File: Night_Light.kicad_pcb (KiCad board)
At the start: 2 copper layers, 25.4 x 25.4 mm, 6 parts, among them J1 3V0, Q1 2N3904

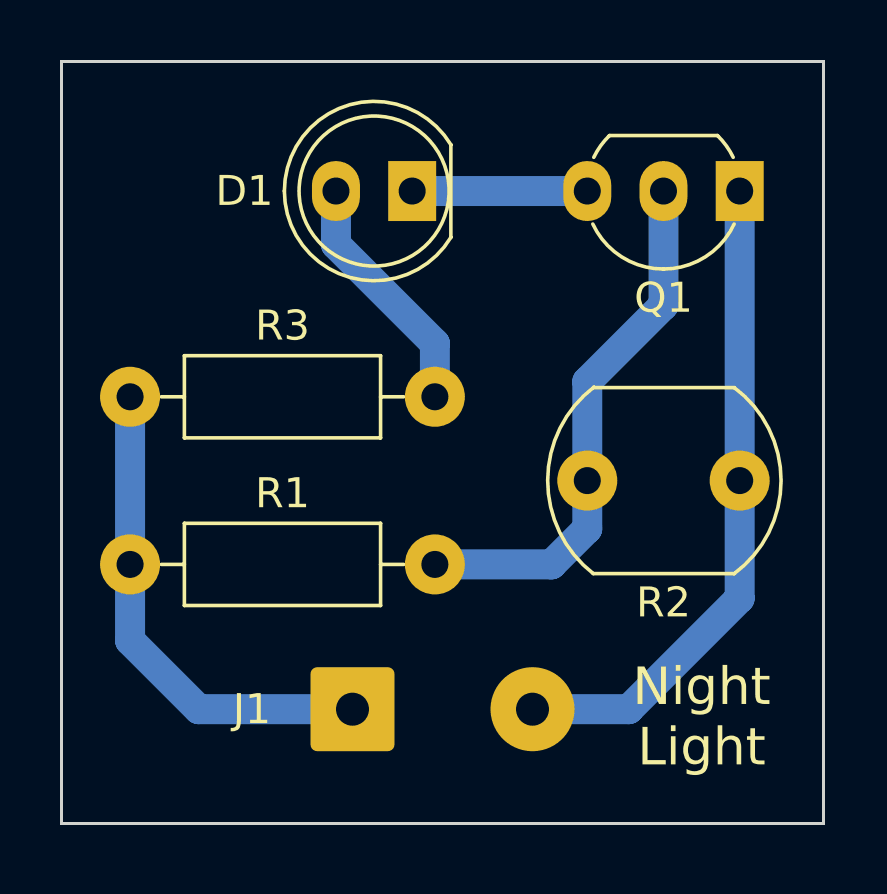
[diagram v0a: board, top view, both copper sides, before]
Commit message: Update silkscreen. Fixes #7, #8, #9, and #11
- Change "D1" label to "LED1". #7
- Make silkscreen text bigger and thicker. #8
- Add "+" and "-" to power pads. #9
- Add LED polarity to silkscreen. #11
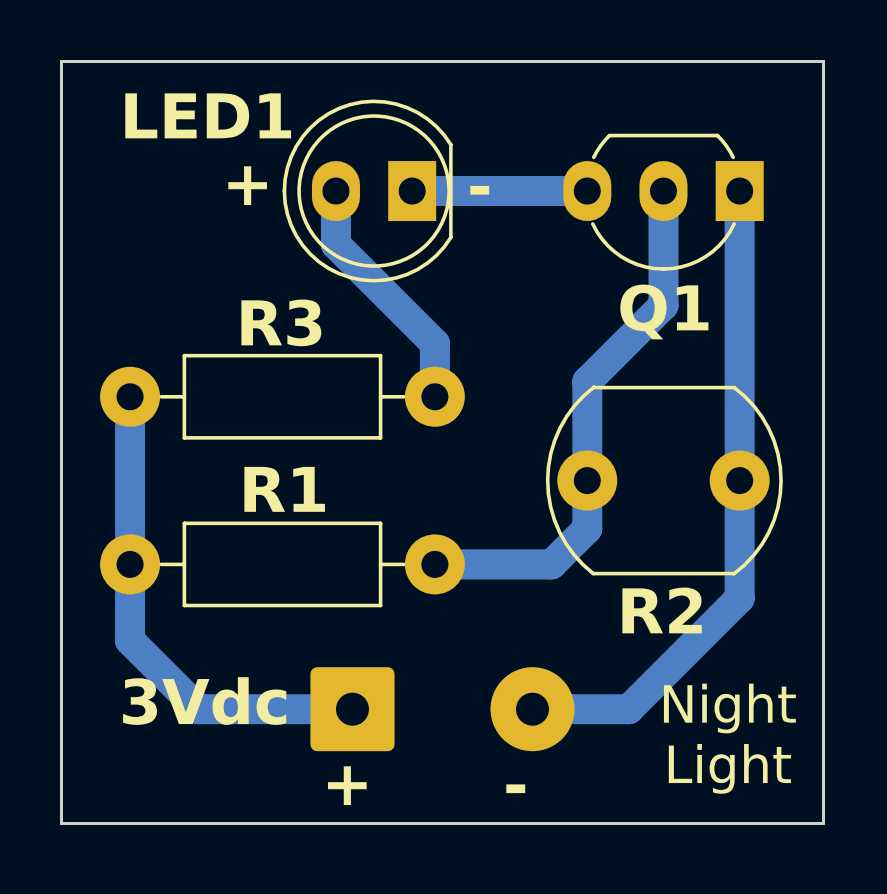
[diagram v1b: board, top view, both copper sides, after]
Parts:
- renumbered D1 to LED1
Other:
- board text added: "+"
- board text added: "-"
- board text added: "3Vdc"
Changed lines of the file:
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@@
     (property "ki_keywords" "LED diode")
     (attr through_hole)
-    (fp_text reference "D1" (at 5.593 0) (layer "F.SilkS")
-        (effects (font (size 1 1) (thickness 0.1524)))
+    (fp_text reference "LED1" (at 6.823 2.45) (layer "F.SilkS")
+        (effects (font (size 1.5 1.5) (thickness 0.25) bold))
     )
     (fp_text value "White" (at 1.27 3.96) (layer "F.Fab")
@@
     (property "ki_keywords" "R res resistor")
     (attr through_hole)
-    (fp_text reference "R3" (at 5.08 -2.37) (layer "F.SilkS")
-        (effects (font (size 1 1) (thickness 0.1524)))
+    (fp_text reference "R3" (at 5.03 -2.408) (layer "F.SilkS")
+        (effects (font (size 1.5 1.5) (thickness 0.25) bold))
     )
     (fp_text value "100R" (at 5.08 2.37) (layer "F.Fab")
@@
     (property "ki_keywords" "transistor NPN")
     (attr through_hole)
-    (fp_text reference "Q1" (at 2.54 -3.56 180) (layer "F.SilkS")
-        (effects (font (size 1 1) (thickness 0.1524)))
+    (fp_text reference "Q1" (at 2.49 -3.95 180) (layer "F.SilkS")
+        (effects (font (size 1.5 1.5) (thickness 0.25) bold))
     )
     (fp_text value "2N3904" (at 2.54 2.79 180) (layer "F.Fab")
@@
     (property "ki_keywords" "connector")
     (attr exclude_from_pos_files)
-    (fp_text reference "J1" (at -3.35 0) (layer "F.SilkS")
-        (effects (font (size 1 1) (thickness 0.1524)))
+    (fp_text reference "J1" (at -4.084 -0.022) (layer "F.SilkS") hide
+        (effects (font (size 1.5 1.5) (thickness 0.25) bold))
     )
     (fp_text value "3V0" (at 3 2.75) (layer "F.Fab")
@@
     (property "ki_keywords" "R res resistor")
     (attr through_hole)
-    (fp_text reference "R1" (at 5.08 -2.37) (layer "F.SilkS")
-        (effects (font (size 1 1) (thickness 0.1524)))
+    (fp_text reference "R1" (at 5.13 -2.446) (layer "F.SilkS")
+        (effects (font (size 1.5 1.5) (thickness 0.25) bold))
     )
     (fp_text value "10K" (at 5.08 2.37) (layer "F.Fab")
@@
     (property "ki_keywords" "resistor variable light sensitive opto LDR")
     (attr through_hole)
-    (fp_text reference "R2" (at 2.54 4.064) (layer "F.SilkS")
-        (effects (font (size 1 1) (thickness 0.1524)))
+    (fp_text reference "R2" (at 2.49 4.398) (layer "F.SilkS")
+        (effects (font (size 1.5 1.5) (thickness 0.25) bold))
     )
     (fp_text value "8K-200K" (at 2.54 4.06) (layer "F.Fab")
@@
     (effects (font (size 1 1) (thickness 0.1524)) (justify mirror))
   )
-  (gr_text "Night\nLight" (at 148.336 98.044) (layer "F.SilkS")
+  (gr_text "+" (at 135.666 101.168) (layer "F.SilkS")
+    (effects (font (size 1.5 1.5) (thickness 0.25) bold) (justify left bottom))
+  )
+  (gr_text "-" (at 141.716 101.218) (layer "F.SilkS")
+    (effects (font (size 1.5 1.5) (thickness 0.25) bold) (justify left bottom))
+  )
+  (gr_text "Night\nLight" (at 149.216 98.668) (layer "F.SilkS")
     (effects (font (size 1.25 1.25) (thickness 0.2)))
   )
+  (gr_text "3Vdc" (at 128.916 98.468) (layer "F.SilkS")
+    (effects (font (size 1.5 1.5) (thickness 0.25) bold) (justify left bottom))
+  )
+  (gr_text "-" (at 140.516 81.268) (layer "F.SilkS")
+    (effects (font (size 1.5 1.5) (thickness 0.25) bold) (justify left bottom))
+  )
+  (gr_text "+" (at 134.066 81.168) (layer "F.SilkS")
+    (effects (font (size 1.5 1.5) (thickness 0.25) bold) (justify left bottom mirror))
+  )
   (segment (start 138.689 80.518) (end 144.526 80.518) (width 1) (layer "B.Cu") (net 1))

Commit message: Update version to 1.1.0
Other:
- board text added: "v1.1.0"
- board text removed: "v1.0.0"
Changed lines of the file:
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@@
   (title_block
     (title "Night Light")
-    (date "2023-02-14")
-    (rev "1.0.0")
+    (date "2023-04-16")
+    (rev "1.1.0")
     (company "Julian Jayhawks")
     (comment 1 "Zach \"Chef\" Dribin")
@@
   (gr_rect (start 127 76.2) (end 152.4 101.6)
     (stroke (width 0.1) (type solid)) (fill none) (layer "Edge.Cuts"))
-  (gr_text "v1.0.0" (at 148.336 98.044) (layer "B.SilkS")
+  (gr_text "v1.1.0" (at 148.336 98.044) (layer "B.SilkS")
     (effects (font (size 1 1) (thickness 0.1524)) (justify mirror))
   )

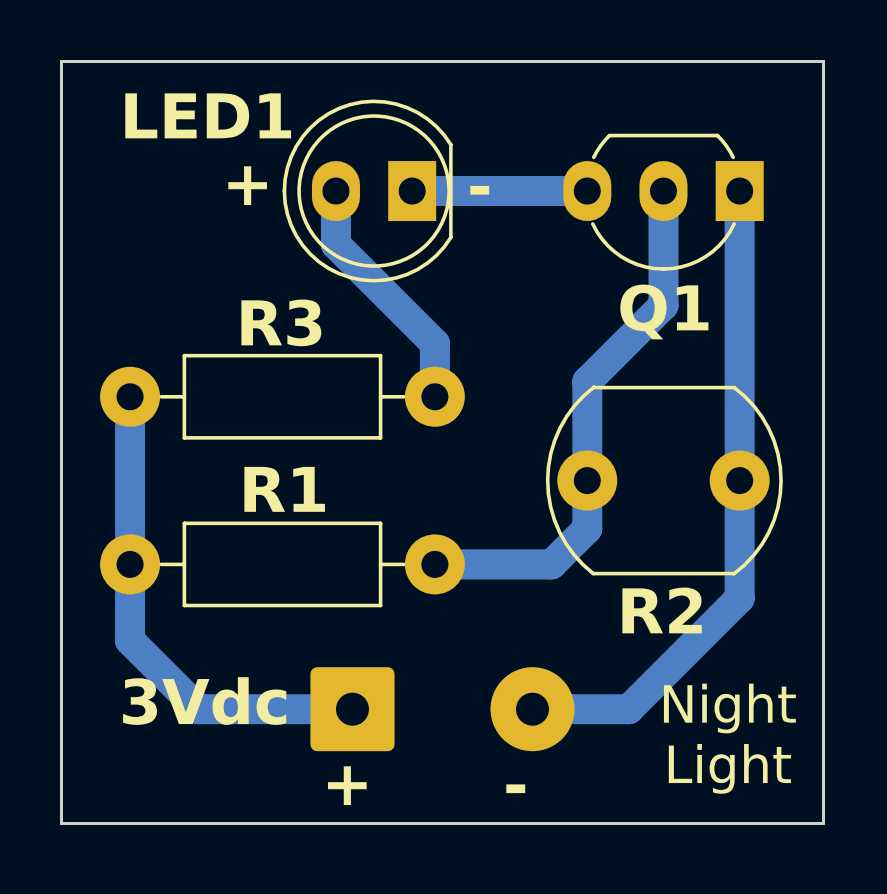
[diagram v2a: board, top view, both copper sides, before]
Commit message: Change R3 and add resistor values to silkscreen
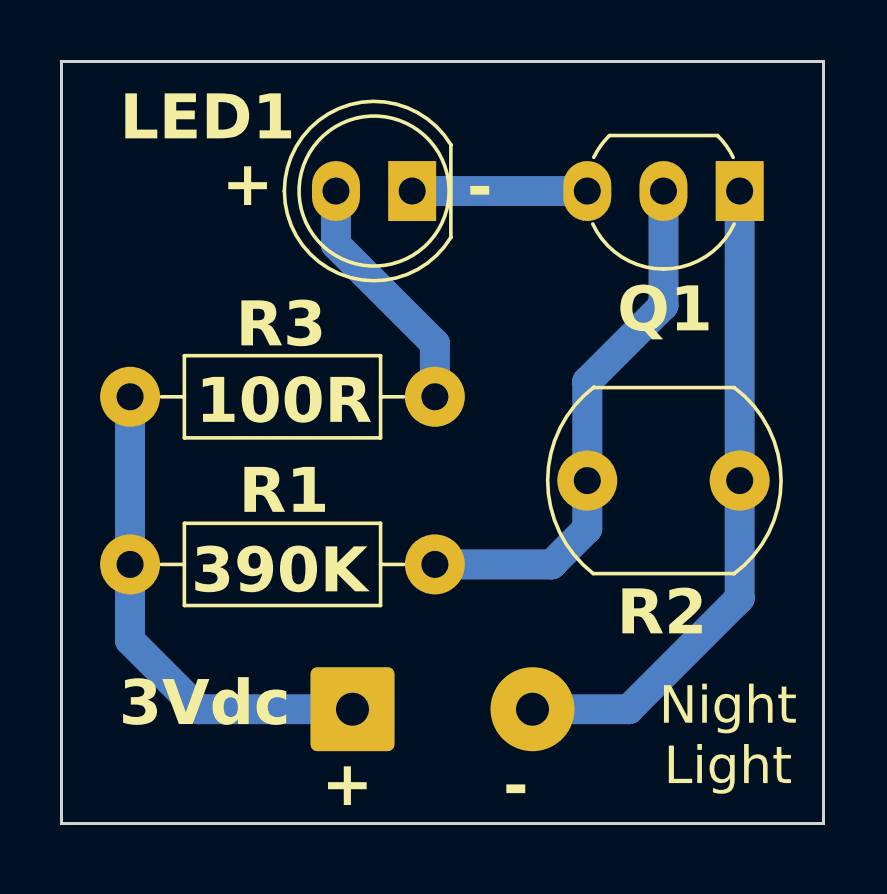
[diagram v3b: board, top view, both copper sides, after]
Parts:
- R1: value 10K -> 390K
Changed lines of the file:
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@@
         (effects (font (size 1.5 1.5) (thickness 0.25) bold))
     )
-    (fp_text value "100R" (at 5.08 2.37) (layer "F.Fab")
-        (effects (font (size 1 1) (thickness 0.15)))
+    (fp_text value "100R" (at 5.13 0.142) (layer "F.SilkS")
+        (effects (font (size 1.5 1.5) (thickness 0.25) bold))
     )
     (fp_text user "${REFERENCE}" (at 5.08 0) (layer "F.Fab")
@@
         (effects (font (size 1.5 1.5) (thickness 0.25) bold))
     )
-    (fp_text value "10K" (at 5.08 2.37) (layer "F.Fab")
-        (effects (font (size 1 1) (thickness 0.15)))
+    (fp_text value "390K" (at 4.98 0.204) (layer "F.SilkS")
+        (effects (font (size 1.5 1.5) (thickness 0.25) bold))
     )
     (fp_text user "${REFERENCE}" (at 5.08 0) (layer "F.Fab")

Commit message: Copy all updated footprints into a project footprint library, to avoid DRC warnings
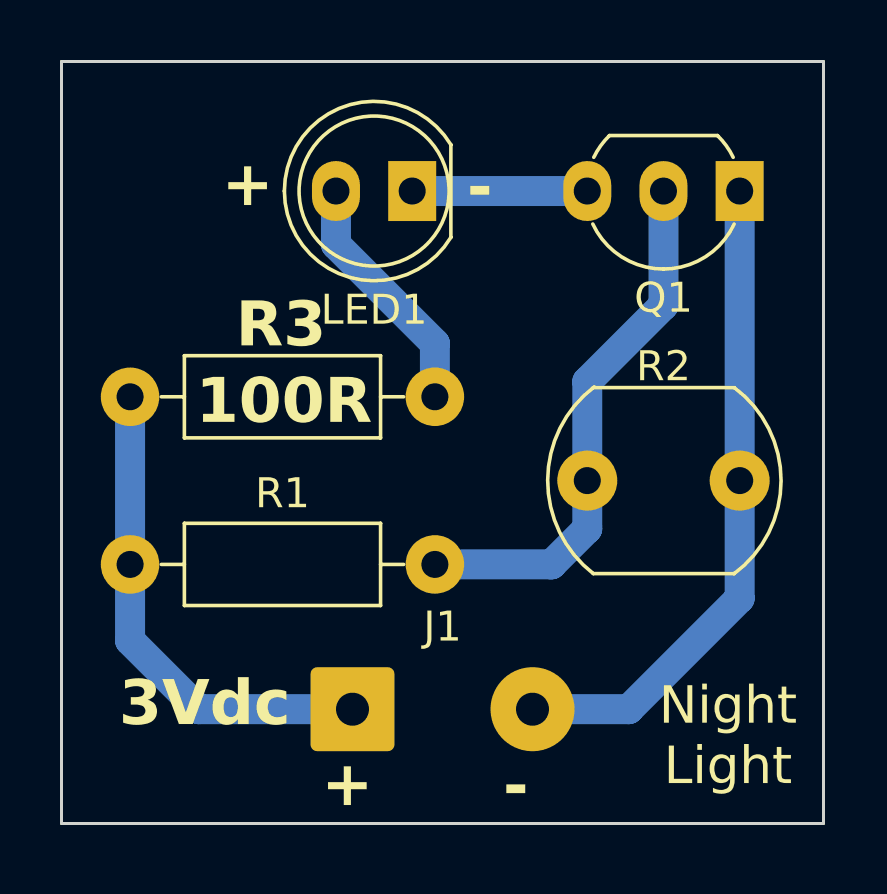
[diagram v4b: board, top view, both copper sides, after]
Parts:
- J1: footprint Connector_Wire:SolderWire-1.5sqmm_1x02_P6mm_D1.7mm_OD3mm -> 00_Project:SolderWire-1.5sqmm_1x02_P6mm_D1.7mm_OD3mm
- LED1: footprint LED_THT:LED_D5.0mm_Clear -> 00_Project:LED_D5.0mm_Clear
- Q1: footprint Package_TO_SOT_THT:TO-92_Inline_Wide -> 00_Project:TO-92_Inline_Wide
- R1, R3: footprint Resistor_THT:R_Axial_DIN0207_L6.3mm_D2.5mm_P10.16mm_Horizontal -> 00_Project:R_Axial_DIN0207_L6.3mm_D2.5mm_P10.16mm_Horizontal
- R2: footprint OptoDevice:R_LDR_7x6mm_P5.1mm_Vertical -> 00_Project:R_LDR_7x6mm_P5.1mm_Vertical
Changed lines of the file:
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@@
   (net 4 "GND")
   (net 5 "/Base")
-  (footprint "LED_THT:LED_D5.0mm_Clear" (layer "F.Cu")
+  (footprint "00_Project:LED_D5.0mm_Clear" (layer "F.Cu")
     (at 138.689 80.518 180)
     (descr "LED, diameter 5.0mm, 2 pins, http://cdn-reichelt.de/documents/datenblatt/A500/LL-504BC2E-009.pdf")
@@
     (property "ki_keywords" "LED diode")
     (attr through_hole)
-    (fp_text reference "LED1" (at 6.823 2.45) (layer "F.SilkS")
-        (effects (font (size 1.5 1.5) (thickness 0.25) bold))
-    )
-    (fp_text value "White" (at 1.27 3.96) (layer "F.Fab")
-        (effects (font (size 1 1) (thickness 0.15)))
-    )
-    (fp_text user "${REFERENCE}" (at 1.25 0) (layer "F.Fab")
+    (fp_text reference "LED1" (at 1.27 -3.96 180) (layer "F.SilkS")
+        (effects (font (size 1 1) (thickness 0.15)))
+    )
+    (fp_text value "White" (at 1.27 3.96 180) (layer "F.Fab")
+        (effects (font (size 1 1) (thickness 0.15)))
+    )
+    (fp_text user "${REFERENCE}" (at 1.25 0 180) (layer "F.Fab")
         (effects (font (size 0.8 0.8) (thickness 0.2)))
     )
@@
     )
   )
-  (footprint "Resistor_THT:R_Axial_DIN0207_L6.3mm_D2.5mm_P10.16mm_Horizontal" (layer "F.Cu")
+  (footprint "00_Project:R_Axial_DIN0207_L6.3mm_D2.5mm_P10.16mm_Horizontal" (layer "F.Cu")
     (at 129.286 87.376)
     (descr "Resistor, Axial_DIN0207 series, Axial, Horizontal, pin pitch=10.16mm, 0.25W = 1/4W, length*diameter=6.3*2.5mm^2, http://cdn-reichelt.de/documents/datenblatt/B400/1_4W%23YAG.pdf")
@@
     (fp_line (start 10.16 0) (end 8.23 0)
       (stroke (width 0.1) (type solid)) (layer "F.Fab"))
-    (pad "1" thru_hole circle (at 0 0) (size 2 2) (drill 0.9) (layers "*.Cu" "*.Mask")
+    (pad "1" thru_hole circle (at 0 0) (size 1.95 1.95) (drill 0.9) (layers "*.Cu" "*.Mask")
       (net 3 "+3V0") (pintype "passive"))
-    (pad "2" thru_hole circle (at 10.16 0) (size 2 2) (drill 0.9) (layers "*.Cu" "*.Mask")
+    (pad "2" thru_hole circle (at 10.16 0) (size 1.95 1.95) (drill 0.9) (layers "*.Cu" "*.Mask")
       (net 2 "/LED +") (pintype "passive"))
     (model "${KICAD6_3DMODEL_DIR}/Resistor_THT.3dshapes/R_Axial_DIN0207_L6.3mm_D2.5mm_P10.16mm_Horizontal.wrl"
@@
     )
   )
-  (footprint "Package_TO_SOT_THT:TO-92_Inline_Wide" (layer "F.Cu")
+  (footprint "00_Project:TO-92_Inline_Wide" (layer "F.Cu")
     (at 149.606 80.518 180)
     (descr "TO-92 leads in-line, wide, drill 0.75mm (see NXP sot054_po.pdf)")
@@
     (property "ki_keywords" "transistor NPN")
     (attr through_hole)
-    (fp_text reference "Q1" (at 2.49 -3.95 180) (layer "F.SilkS")
-        (effects (font (size 1.5 1.5) (thickness 0.25) bold))
+    (fp_text reference "Q1" (at 2.54 -3.56 180) (layer "F.SilkS")
+        (effects (font (size 1 1) (thickness 0.15)))
     )
     (fp_text value "2N3904" (at 2.54 2.79 180) (layer "F.Fab")
@@
     )
   )
-  (footprint "Connector_Wire:SolderWire-1.5sqmm_1x02_P6mm_D1.7mm_OD3mm" (layer "F.Cu")
+  (footprint "00_Project:SolderWire-1.5sqmm_1x02_P6mm_D1.7mm_OD3mm" (layer "F.Cu")
     (at 136.7 97.79)
     (descr "Soldered wire connection, for 2 times 1.5 mm² wires, basic insulation, conductor diameter 1.7mm, outer diameter 3mm, size source Multi-Contact FLEXI-E 1.5 (https://ec.staubli.com/AcroFiles/Catalogues/TM_Cab-Main-11014119_(en)_hi.pdf), bend radius 3 times outer diameter, generated with kicad-footprint-generator")
@@
     (property "ki_description" "Generic connector, single row, 01x02, script generated")
     (property "ki_keywords" "connector")
-    (attr exclude_from_pos_files)
-    (fp_text reference "J1" (at -4.084 -0.022) (layer "F.SilkS") hide
-        (effects (font (size 1.5 1.5) (thickness 0.25) bold))
+    (attr exclude_from_pos_files exclude_from_bom)
+    (fp_text reference "J1" (at 3 -2.75) (layer "F.SilkS")
+        (effects (font (size 1 1) (thickness 0.15)))
     )
     (fp_text value "3V0" (at 3 2.75) (layer "F.Fab")
@@
     )
   )
-  (footprint "Resistor_THT:R_Axial_DIN0207_L6.3mm_D2.5mm_P10.16mm_Horizontal" (layer "F.Cu")
+  (footprint "00_Project:R_Axial_DIN0207_L6.3mm_D2.5mm_P10.16mm_Horizontal" (layer "F.Cu")
     (at 129.286 92.964)
     (descr "Resistor, Axial_DIN0207 series, Axial, Horizontal, pin pitch=10.16mm, 0.25W = 1/4W, length*diameter=6.3*2.5mm^2, http://cdn-reichelt.de/documents/datenblatt/B400/1_4W%23YAG.pdf")
@@
     (property "ki_keywords" "R res resistor")
     (attr through_hole)
-    (fp_text reference "R1" (at 5.13 -2.446) (layer "F.SilkS")
-        (effects (font (size 1.5 1.5) (thickness 0.25) bold))
-    )
-    (fp_text value "390K" (at 4.98 0.204) (layer "F.SilkS")
-        (effects (font (size 1.5 1.5) (thickness 0.25) bold))
+    (fp_text reference "R1" (at 5.08 -2.37) (layer "F.SilkS")
+        (effects (font (size 1 1) (thickness 0.15)))
+    )
+    (fp_text value "390K" (at 5.08 2.37) (layer "F.Fab")
+        (effects (font (size 1 1) (thickness 0.15)))
     )
     (fp_text user "${REFERENCE}" (at 5.08 0) (layer "F.Fab")
@@
     (fp_line (start 10.16 0) (end 8.23 0)
       (stroke (width 0.1) (type solid)) (layer "F.Fab"))
-    (pad "1" thru_hole circle (at 0 0) (size 2 2) (drill 0.9) (layers "*.Cu" "*.Mask")
+    (pad "1" thru_hole circle (at 0 0) (size 1.95 1.95) (drill 0.9) (layers "*.Cu" "*.Mask")
       (net 3 "+3V0") (pintype "passive"))
-    (pad "2" thru_hole circle (at 10.16 0) (size 2 2) (drill 0.9) (layers "*.Cu" "*.Mask")
+    (pad "2" thru_hole circle (at 10.16 0) (size 1.95 1.95) (drill 0.9) (layers "*.Cu" "*.Mask")
       (net 5 "/Base") (pintype "passive"))
     (model "${KICAD6_3DMODEL_DIR}/Resistor_THT.3dshapes/R_Axial_DIN0207_L6.3mm_D2.5mm_P10.16mm_Horizontal.wrl"
@@
     )
   )
-  (footprint "OptoDevice:R_LDR_7x6mm_P5.1mm_Vertical" (layer "F.Cu")
+  (footprint "00_Project:R_LDR_7x6mm_P5.1mm_Vertical" (layer "F.Cu")
     (at 144.526 90.17)
     (descr "Resistor, LDR 7x6mm")
@@
     (property "ki_keywords" "resistor variable light sensitive opto LDR")
     (attr through_hole)
-    (fp_text reference "R2" (at 2.49 4.398) (layer "F.SilkS")
-        (effects (font (size 1.5 1.5) (thickness 0.25) bold))
+    (fp_text reference "R2" (at 2.54 -3.81) (layer "F.SilkS")
+        (effects (font (size 1 1) (thickness 0.15)))
     )
     (fp_text value "8K-200K" (at 2.54 4.06) (layer "F.Fab")
